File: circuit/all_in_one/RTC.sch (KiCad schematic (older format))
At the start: 0 parts

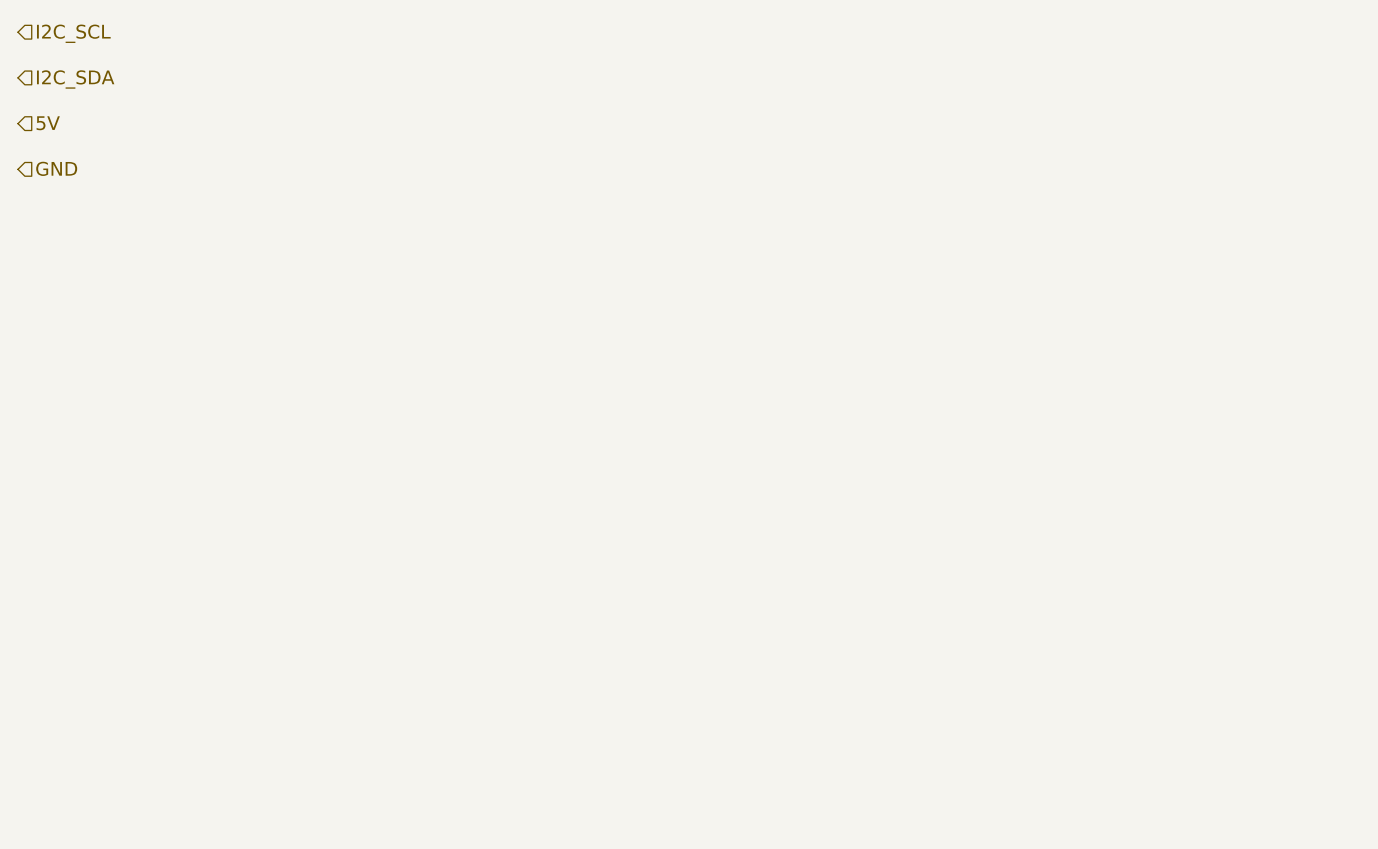
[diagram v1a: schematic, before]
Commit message: [All in one circuit]Add DS1307
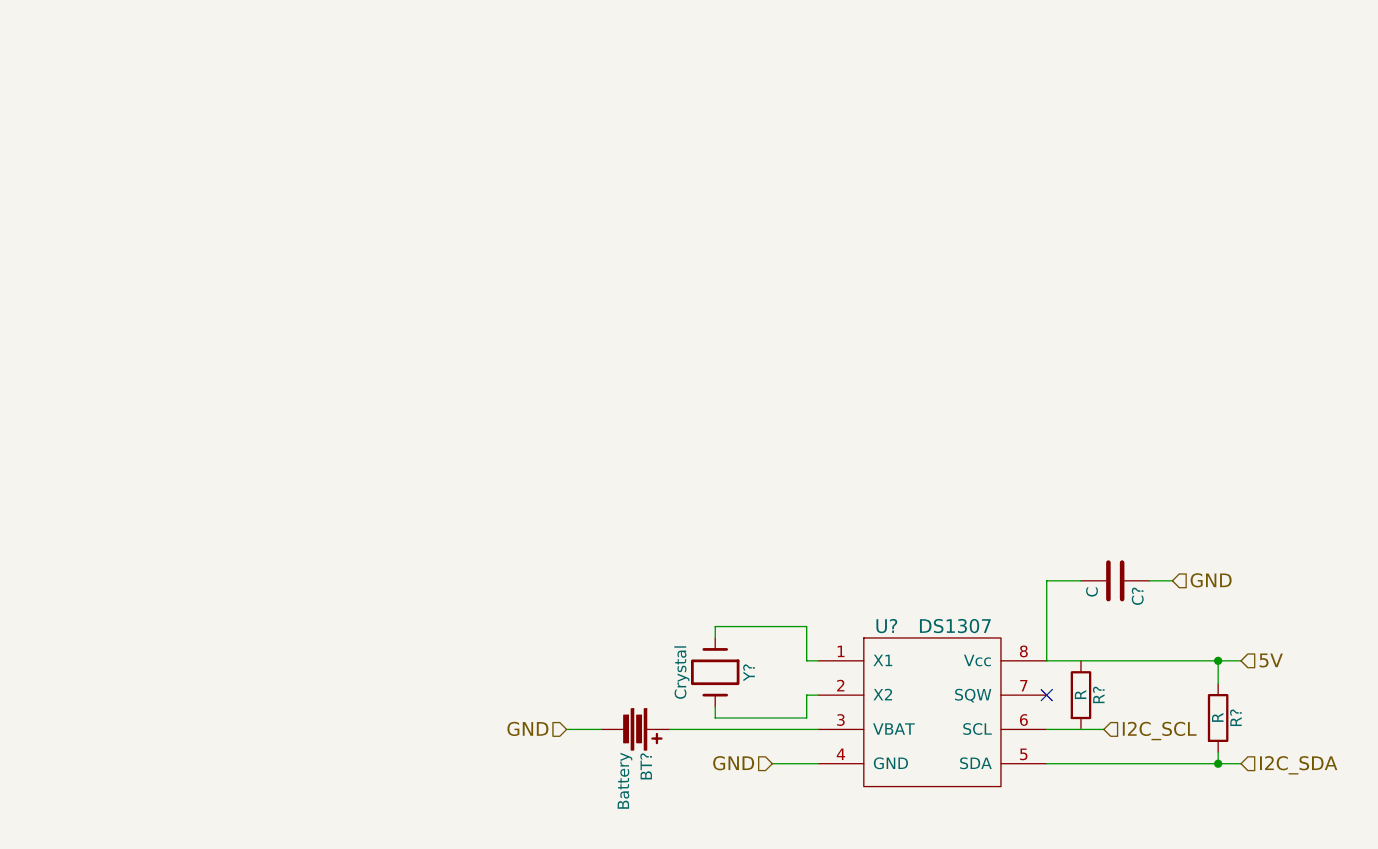
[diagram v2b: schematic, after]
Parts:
- added BT?: Battery, symbol Battery
- added C?: C, symbol C
- added R? (x2): R, symbol R
- added U?: DS1307, symbol DS1307
- added Y?: Crystal, symbol Crystal
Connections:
- net 5V: now also C?.2, R?.1, U?.8 (Vcc)
- net GND: now also BT?.2, C?.1, U?.4 (GND)
- net I2C_SCL: now also U?.6 (SCL)
- net I2C_SDA: now also R?.2, U?.5 (SDA)
- new net: U?.1 (X1), Y?.1
- new net: U?.2 (X2), Y?.2
- new net: BT?.1, U?.3 (VBAT)
- no-connect marks 0 -> 1
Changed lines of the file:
@@
 Comment4 ""
 $EndDescr
-Text HLabel 1800 1150 2    60   Input ~ 0
+Text HLabel 6550 4200 2    60   Input ~ 0
 I2C_SCL
-Text HLabel 1800 1350 2    60   Input ~ 0
+Text HLabel 7150 4350 2    60   Input ~ 0
 I2C_SDA
-Text HLabel 1800 1550 2    60   Input ~ 0
+Text HLabel 7150 3900 2    60   Input ~ 0
 5V
-Text HLabel 1800 1750 2    60   Input ~ 0
+Text HLabel 6850 3550 2    60   Input ~ 0
 GND
+$Comp
+L DS1307 U?
+U 1 1 5647D894
+P 5800 4150
+F 0 "U?" H 5600 4550 60  0000 C CNN
+F 1 "DS1307" H 5900 4550 60  0000 C CNN
+F 2 "" H 5600 4550 60  0000 C CNN
+F 3 "" H 5600 4550 60  0000 C CNN
+	1    5800 4150
+	1    0    0    -1
+$EndComp
+$Comp
+L C C?
+U 1 1 5647D9A5
+P 6600 3550
+F 0 "C?" H 6625 3650 50  0000 L CNN
+F 1 "C" H 6625 3450 50  0000 L CNN
+F 2 "" H 6638 3400 30  0000 C CNN
+F 3 "" H 6600 3550 60  0000 C CNN
+	1    6600 3550
+	0    1    1    0
+$EndComp
+Wire Wire Line
+	6750 3550 6850 3550
+Wire Wire Line
+	6300 3900 7150 3900
+Wire Wire Line
+	6450 3550 6300 3550
+Wire Wire Line
+	6300 3550 6300 3900
+NoConn ~ 6300 4050
+Wire Wire Line
+	6300 4200 6550 4200
+Wire Wire Line
+	6300 4350 7150 4350
+Text HLabel 5100 4350 0    60   Input ~ 0
+GND
+Wire Wire Line
+	5100 4350 5300 4350
+$Comp
+L Crystal Y?
+U 1 1 5647DAEC
+P 4850 3950
+F 0 "Y?" H 4850 4100 50  0000 C CNN
+F 1 "Crystal" H 4850 3800 50  0000 C CNN
+F 2 "" H 4850 3950 60  0000 C CNN
+F 3 "" H 4850 3950 60  0000 C CNN
+	1    4850 3950
+	0    1    1    0
+$EndComp
+Wire Wire Line
+	4850 3800 4850 3750
+Wire Wire Line
+	4850 3750 5250 3750
+Wire Wire Line
+	5250 3750 5250 3900
+Wire Wire Line
+	5250 3900 5300 3900
+Wire Wire Line
+	5300 4050 5250 4050
+Wire Wire Line
+	5250 4050 5250 4150
+Wire Wire Line
+	5250 4150 4850 4150
+Wire Wire Line
+	4850 4150 4850 4100
+$Comp
+L Battery BT?
+U 1 1 5647DBD2
+P 4500 4200
+F 0 "BT?" H 4600 4250 50  0000 L CNN
+F 1 "Battery" H 4600 4150 50  0000 L CNN
+F 2 "" V 4500 4240 60  0000 C CNN
+F 3 "" V 4500 4240 60  0000 C CNN
+	1    4500 4200
+	0    1    1    0
+$EndComp
+Wire Wire Line
+	5300 4200 4650 4200
+Text HLabel 4200 4200 0    60   Input ~ 0
+GND
+Wire Wire Line
+	4200 4200 4350 4200
+$Comp
+L R R?
+U 1 1 5647E0E9
+P 7050 4150
+F 0 "R?" V 7130 4150 50  0000 C CNN
+F 1 "R" V 7050 4150 50  0000 C CNN
+F 2 "" V 6980 4150 30  0000 C CNN
+F 3 "" H 7050 4150 30  0000 C CNN
+	1    7050 4150
+	1    0    0    -1
+$EndComp
+Wire Wire Line
+	7050 4000 7050 3900
+Connection ~ 7050 3900
+Wire Wire Line
+	7050 4300 7050 4350
+Connection ~ 7050 4350
+$Comp
+L R R?
+U 1 1 5647E182
+P 6450 4050
+F 0 "R?" V 6530 4050 50  0000 C CNN
+F 1 "R" V 6450 4050 50  0000 C CNN
+F 2 "" V 6380 4050 30  0000 C CNN
+F 3 "" H 6450 4050 30  0000 C CNN
+	1    6450 4050
+	1    0    0    -1
+$EndComp
 $EndSCHEMATC

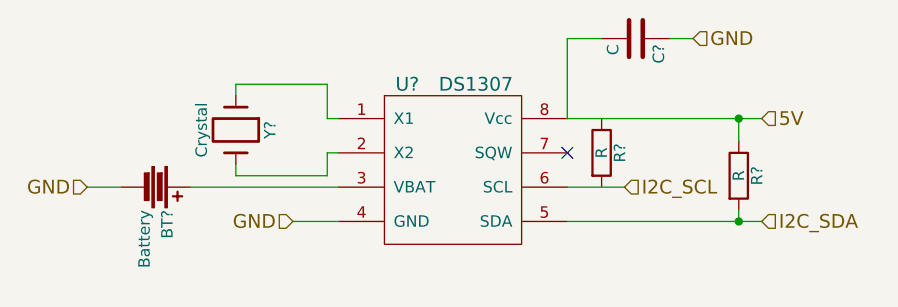
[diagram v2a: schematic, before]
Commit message: [All in one circuit]Arrange the USART pin
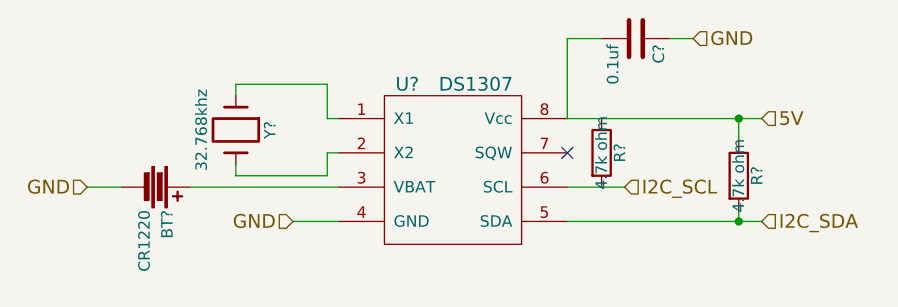
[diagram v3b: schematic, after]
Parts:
- BT?: value Battery -> CR1220
- C?: value C -> 0.1uf
- R? (x2): value R -> 4.7k ohm
- Y?: value Crystal -> 32.768khz
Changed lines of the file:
@@
 P 6600 3550
 F 0 "C?" H 6625 3650 50  0000 L CNN
-F 1 "C" H 6625 3450 50  0000 L CNN
+F 1 "0.1uf" H 6625 3450 50  0000 L CNN
 F 2 "" H 6638 3400 30  0000 C CNN
 F 3 "" H 6600 3550 60  0000 C CNN
@@
 P 4850 3950
 F 0 "Y?" H 4850 4100 50  0000 C CNN
-F 1 "Crystal" H 4850 3800 50  0000 C CNN
+F 1 "32.768khz" H 4850 3800 50  0000 C CNN
 F 2 "" H 4850 3950 60  0000 C CNN
 F 3 "" H 4850 3950 60  0000 C CNN
@@
 P 4500 4200
 F 0 "BT?" H 4600 4250 50  0000 L CNN
-F 1 "Battery" H 4600 4150 50  0000 L CNN
+F 1 "CR1220" H 4600 4150 50  0000 L CNN
 F 2 "" V 4500 4240 60  0000 C CNN
 F 3 "" V 4500 4240 60  0000 C CNN
@@
 P 7050 4150
 F 0 "R?" V 7130 4150 50  0000 C CNN
-F 1 "R" V 7050 4150 50  0000 C CNN
+F 1 "4.7k ohm" V 7050 4150 50  0000 C CNN
 F 2 "" V 6980 4150 30  0000 C CNN
 F 3 "" H 7050 4150 30  0000 C CNN
@@
 P 6450 4050
 F 0 "R?" V 6530 4050 50  0000 C CNN
-F 1 "R" V 6450 4050 50  0000 C CNN
+F 1 "4.7k ohm" V 6450 4050 50  0000 C CNN
 F 2 "" V 6380 4050 30  0000 C CNN
 F 3 "" H 6450 4050 30  0000 C CNN

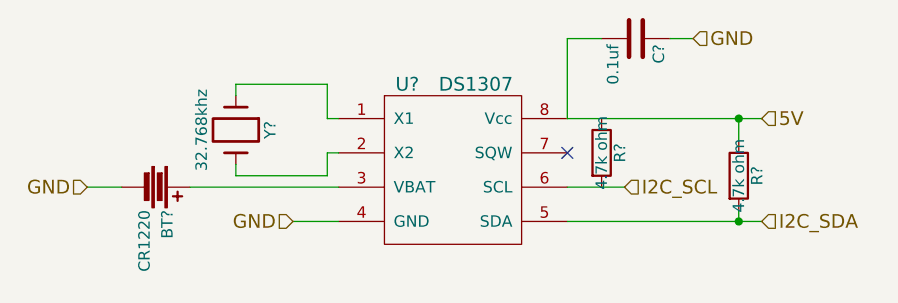
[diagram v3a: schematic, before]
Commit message: [All in one]Define part of compoment's footprint
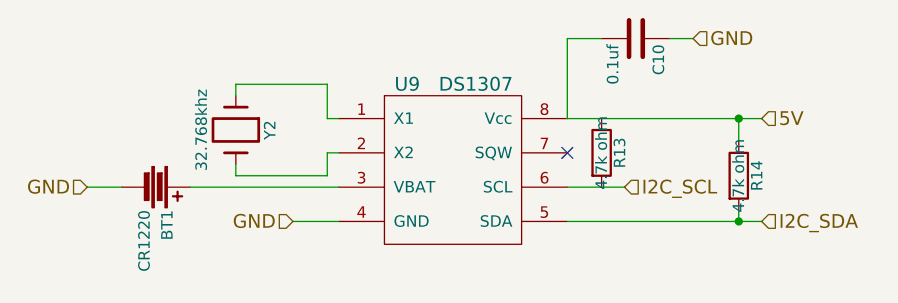
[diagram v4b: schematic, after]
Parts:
- BT1: renamed from BT?; footprint (none) -> Connect:CR2032H
- U9: renamed from U?; footprint (none) -> Power_Integrations:SO-8
- Y2: renamed from Y?; footprint (none) -> Crystals:Crystal_Round_Vertical_2mm
- gave numbers to parts that had none: 3
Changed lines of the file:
@@
 GND
 $Comp
-L DS1307 U?
+L DS1307 U9
 U 1 1 5647D894
 P 5800 4150
-F 0 "U?" H 5600 4550 60  0000 C CNN
+F 0 "U9" H 5600 4550 60  0000 C CNN
 F 1 "DS1307" H 5900 4550 60  0000 C CNN
-F 2 "" H 5600 4550 60  0000 C CNN
+F 2 "Power_Integrations:SO-8" H 5600 4550 60  0001 C CNN
 F 3 "" H 5600 4550 60  0000 C CNN
 	1    5800 4150
@@
 $EndComp
 $Comp
-L C C?
+L C C10
 U 1 1 5647D9A5
 P 6600 3550
-F 0 "C?" H 6625 3650 50  0000 L CNN
+F 0 "C10" H 6625 3650 50  0000 L CNN
 F 1 "0.1uf" H 6625 3450 50  0000 L CNN
-F 2 "" H 6638 3400 30  0000 C CNN
+F 2 "" H 6638 3400 30  0001 C CNN
 F 3 "" H 6600 3550 60  0000 C CNN
 	1    6600 3550
@@
 	5100 4350 5300 4350
 $Comp
-L Crystal Y?
+L Crystal Y2
 U 1 1 5647DAEC
 P 4850 3950
-F 0 "Y?" H 4850 4100 50  0000 C CNN
+F 0 "Y2" H 4850 4100 50  0000 C CNN
 F 1 "32.768khz" H 4850 3800 50  0000 C CNN
-F 2 "" H 4850 3950 60  0000 C CNN
+F 2 "Crystals:Crystal_Round_Vertical_2mm" H 4850 3950 60  0001 C CNN
 F 3 "" H 4850 3950 60  0000 C CNN
 	1    4850 3950
@@
 	4850 4150 4850 4100
 $Comp
-L Battery BT?
+L Battery BT1
 U 1 1 5647DBD2
 P 4500 4200
-F 0 "BT?" H 4600 4250 50  0000 L CNN
+F 0 "BT1" H 4600 4250 50  0000 L CNN
 F 1 "CR1220" H 4600 4150 50  0000 L CNN
-F 2 "" V 4500 4240 60  0000 C CNN
+F 2 "Connect:CR2032H" V 4500 4240 60  0001 C CNN
 F 3 "" V 4500 4240 60  0000 C CNN
 	1    4500 4200
@@
 	4200 4200 4350 4200
 $Comp
-L R R?
+L R R14
 U 1 1 5647E0E9
 P 7050 4150
-F 0 "R?" V 7130 4150 50  0000 C CNN
+F 0 "R14" V 7130 4150 50  0000 C CNN
 F 1 "4.7k ohm" V 7050 4150 50  0000 C CNN
-F 2 "" V 6980 4150 30  0000 C CNN
+F 2 "" V 6980 4150 30  0001 C CNN
 F 3 "" H 7050 4150 30  0000 C CNN
 	1    7050 4150
@@
 Connection ~ 7050 4350
 $Comp
-L R R?
+L R R13
 U 1 1 5647E182
 P 6450 4050
-F 0 "R?" V 6530 4050 50  0000 C CNN
+F 0 "R13" V 6530 4050 50  0000 C CNN
 F 1 "4.7k ohm" V 6450 4050 50  0000 C CNN
-F 2 "" V 6380 4050 30  0000 C CNN
+F 2 "" V 6380 4050 30  0001 C CNN
 F 3 "" H 6450 4050 30  0000 C CNN
 	1    6450 4050

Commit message: [All in one]Select resister and power jack's footprint
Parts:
- R13, R14: footprint (none) -> Resistors_SMD:R_0805_HandSoldering
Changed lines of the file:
@@
 F 0 "R14" V 7130 4150 50  0000 C CNN
 F 1 "4.7k ohm" V 7050 4150 50  0000 C CNN
-F 2 "" V 6980 4150 30  0001 C CNN
+F 2 "Resistors_SMD:R_0805_HandSoldering" V 6980 4150 30  0001 C CNN
 F 3 "" H 7050 4150 30  0000 C CNN
 	1    7050 4150
@@
 F 0 "R13" V 6530 4050 50  0000 C CNN
 F 1 "4.7k ohm" V 6450 4050 50  0000 C CNN
-F 2 "" V 6380 4050 30  0001 C CNN
+F 2 "Resistors_SMD:R_0805_HandSoldering" V 6380 4050 30  0001 C CNN
 F 3 "" H 6450 4050 30  0000 C CNN
 	1    6450 4050

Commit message: [All in one]Select footprint for capacitors
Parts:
- C10: footprint (none) -> Capacitors_SMD:C_0805_HandSoldering
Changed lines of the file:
@@
 F 0 "C10" H 6625 3650 50  0000 L CNN
 F 1 "0.1uf" H 6625 3450 50  0000 L CNN
-F 2 "" H 6638 3400 30  0001 C CNN
+F 2 "Capacitors_SMD:C_0805_HandSoldering" H 6638 3400 30  0001 C CNN
 F 3 "" H 6600 3550 60  0000 C CNN
 	1    6600 3550

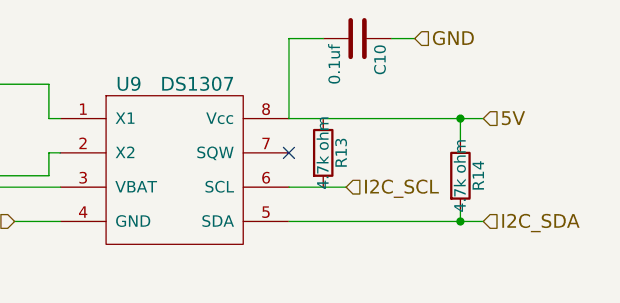
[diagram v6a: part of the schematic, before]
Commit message: Finsihed placing all the components
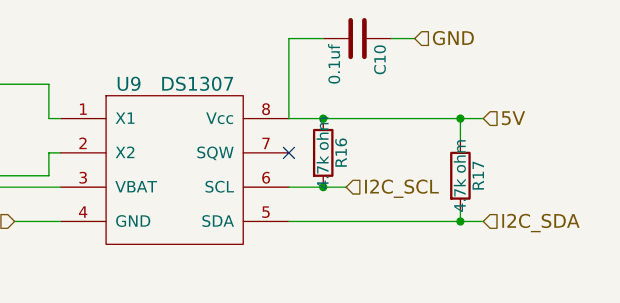
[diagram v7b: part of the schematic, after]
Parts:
- renumbered R13 to R16, R14 to R17
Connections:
- net 5V: now also R16.1
- net I2C_SCL: now also R16.2
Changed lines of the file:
@@
 $Descr A4 11693 8268
 encoding utf-8
-Sheet 4 6
+Sheet 4 5
 Title ""
 Date ""
@@
 	4200 4200 4350 4200
 $Comp
-L R R14
+L R R17
 U 1 1 5647E0E9
 P 7050 4150
-F 0 "R14" V 7130 4150 50  0000 C CNN
+F 0 "R17" V 7130 4150 50  0000 C CNN
 F 1 "4.7k ohm" V 7050 4150 50  0000 C CNN
 F 2 "Resistors_SMD:R_0805_HandSoldering" V 6980 4150 30  0001 C CNN
@@
 Connection ~ 7050 4350
 $Comp
-L R R13
+L R R16
 U 1 1 5647E182
 P 6450 4050
-F 0 "R13" V 6530 4050 50  0000 C CNN
+F 0 "R16" V 6530 4050 50  0000 C CNN
 F 1 "4.7k ohm" V 6450 4050 50  0000 C CNN
 F 2 "Resistors_SMD:R_0805_HandSoldering" V 6380 4050 30  0001 C CNN
@@
 	1    0    0    -1
 $EndComp
+Connection ~ 6450 3900
+Connection ~ 6450 4200
 $EndSCHEMATC

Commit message: More works on PCB layout...
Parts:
- BT1: footprint Connect:CR2032H -> cr1220_smd:cr1220smd
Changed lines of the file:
@@
 F 0 "BT1" H 4600 4250 50  0000 L CNN
 F 1 "CR1220" H 4600 4150 50  0000 L CNN
-F 2 "Connect:CR2032H" V 4500 4240 60  0001 C CNN
+F 2 "cr1220_smd:cr1220smd" V 4500 4240 60  0001 C CNN
 F 3 "" V 4500 4240 60  0000 C CNN
 	1    4500 4200
